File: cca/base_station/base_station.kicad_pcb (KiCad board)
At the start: 2 copper layers, 76.2 x 50.8 mm, 11 parts, among them P1 tstat_ui_conn, P2 tstat_cable_con, U1 RFM69W, U2 DHT22, U3 TEENSY-LC

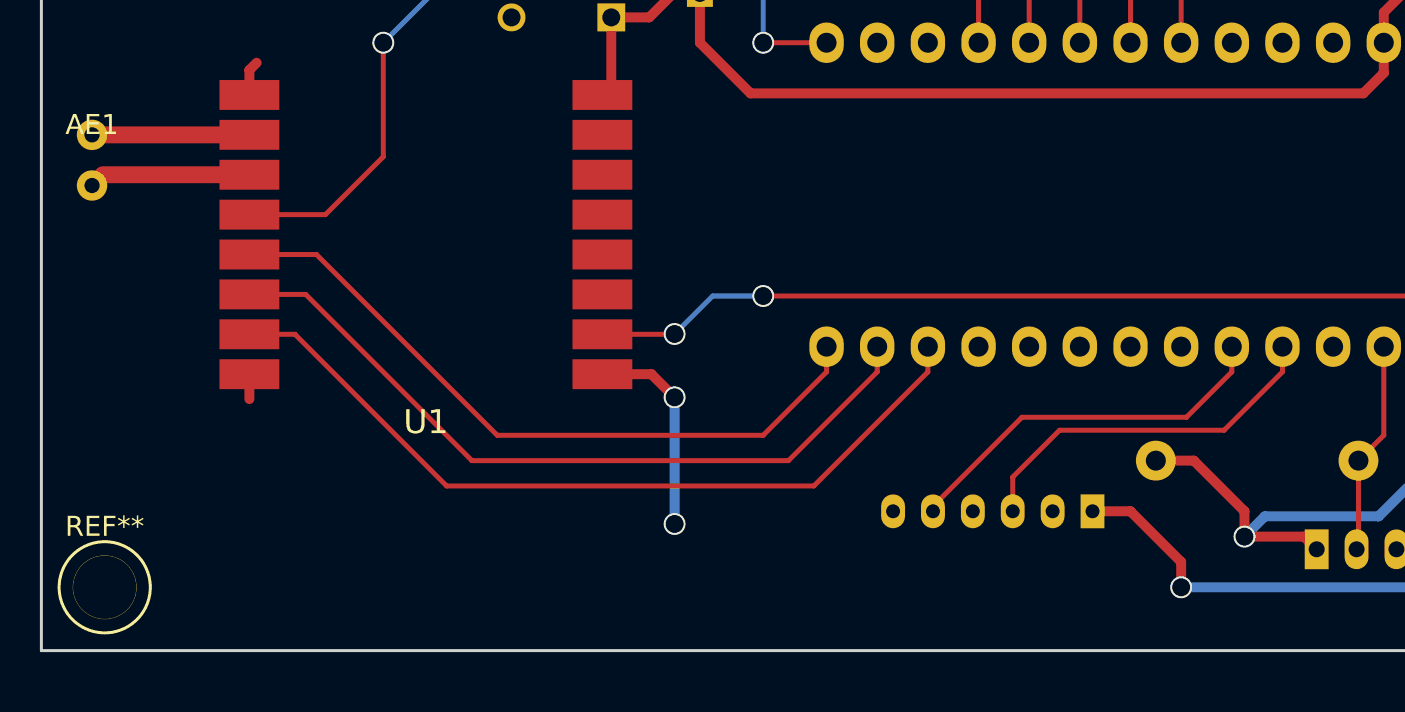
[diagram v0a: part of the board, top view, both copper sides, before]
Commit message: footprint drillholes metric
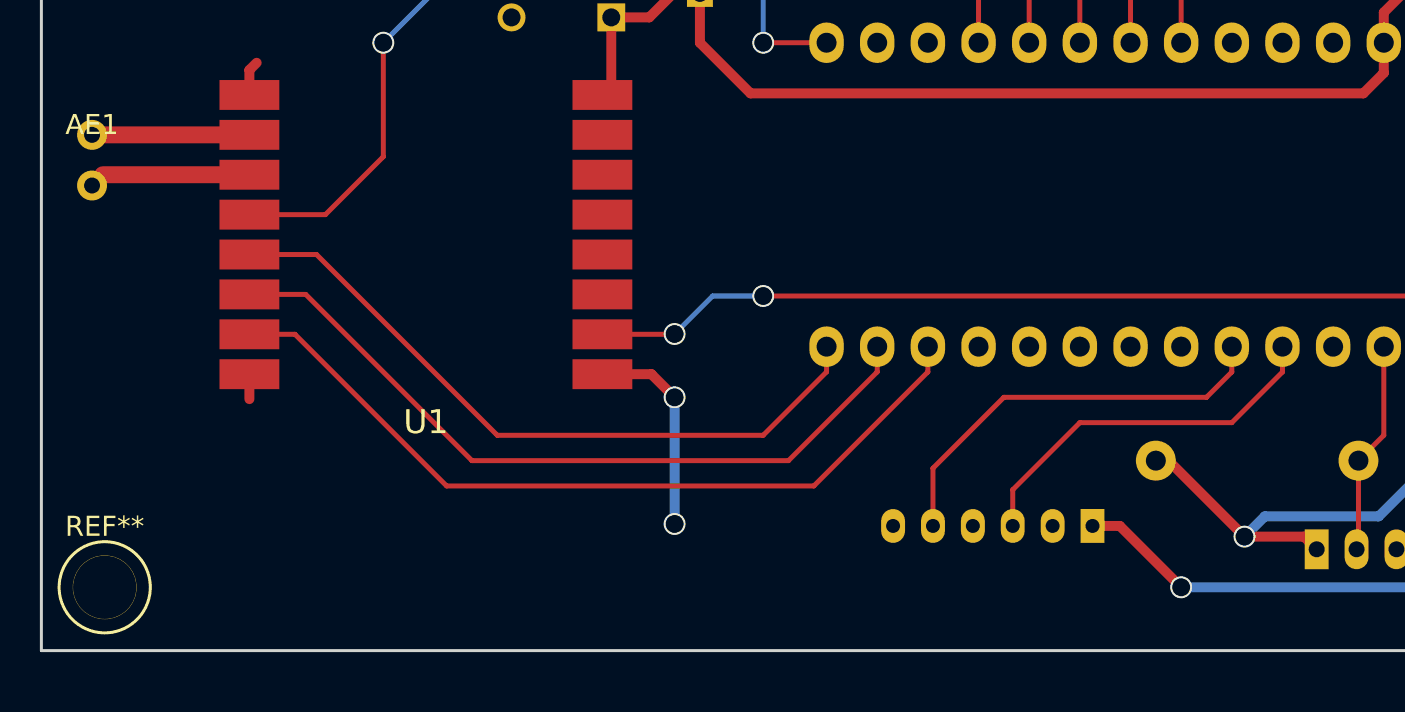
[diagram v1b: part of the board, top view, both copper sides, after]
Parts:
- R1: footprint Resistors_ThroughHole:Resistor_Horizontal_RM10mm -> t_footprints:Resistor_Horizontal_RM10mm
- moved P1 0.73 mm to (78.1, 70.0)
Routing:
- net Net-(P1-Pad5): track 19.3 -> 21.1 mm
- net +5V: track 79.1 -> 78.1 mm
- net +3V3: track 122.8 -> 122.1 mm
